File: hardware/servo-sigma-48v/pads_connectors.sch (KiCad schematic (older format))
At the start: 38 parts, among them J1 CONN_01X02, J3 CONN_01X03, J4 CONN_01X03_MALE, U1 ST1S14, U2 TPS70950, U3 ACS711, U8 TPS70933

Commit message: Updated the footprints
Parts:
- C1, C6, C9: footprint Capacitors_SMD:CP_Elec_10x10 -> Capacitor_SMD:CP_Elec_10x10; symbol device:CP -> servo-sigma-48v-rescue:CP-device
- C10, C12, C13, C37: footprint Capacitors_SMD:C_0603 -> Capacitor_SMD:C_0603_1608Metric; symbol device:C -> servo-sigma-48v-rescue:C-device
- C2, C7: footprint Capacitors_SMD:C_1206 -> Capacitor_SMD:C_1206_3216Metric; symbol device:C -> servo-sigma-48v-rescue:C-device
- C38: footprint Capacitors_SMD:CP_Elec_6.3x7.7 -> Capacitor_SMD:CP_Elec_6.3x7.7; symbol device:CP -> servo-sigma-48v-rescue:CP-device
- C39, C40, C41, C42, C5, C8: footprint Capacitors_SMD:C_0805 -> Capacitor_SMD:C_0805_2012Metric; symbol device:C -> servo-sigma-48v-rescue:C-device
- D2, D3, D5: symbol device:D_Schottky -> servo-sigma-48v-rescue:D_Schottky-device
- J1: symbol conn:CONN_01X02 -> servo-sigma-48v-rescue:CONN_01X02-conn
- J3: symbol conn:CONN_01X03 -> servo-sigma-48v-rescue:CONN_01X03-conn
- J4: footprint Pin_Headers:Pin_Header_Straight_1x03_Pitch2.54mm -> Connector_PinHeader_2.54mm:PinHeader_1x03_P2.54mm_Vertical; symbol conn:CONN_01X03_MALE -> servo-sigma-48v-rescue:CONN_01X03_MALE-conn
- L1: footprint Inductors_SMD:L_Wuerth_WE-TPC-3816 -> Inductor_SMD:L_Wuerth_WE-TPC-3816; symbol device:L -> servo-sigma-48v-rescue:L-device
- R11, R12, R13, R14, R15, R6, R7: footprint Resistors_SMD:R_0603 -> Resistor_SMD:R_0603_1608Metric; symbol device:R -> servo-sigma-48v-rescue:R-device
- U1: footprint Housings_SOIC:SOIC-8-1EP_3.9x4.9mm_Pitch1.27mm -> Package_SO:SOIC-8-1EP_3.9x4.9mm_P1.27mm_EP2.35x2.35mm
- U2, U8: footprint TO_SOT_Packages_SMD:SOT-23-5 -> Package_TO_SOT_SMD:SOT-23-5; symbol regul:TPS793333-EP -> servo-sigma-48v-rescue:TPS793333-EP-regul
- U3: footprint Housings_SOIC:SOIC-8_3.9x4.9mm_Pitch1.27mm -> Package_SO:SOIC-8_3.9x4.9mm_P1.27mm

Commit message: Work on sigmadrive 2.0
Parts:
- removed C10: 100nF 50V, Capacitor_SMD:C_0603_1608Metric, symbol servo-sigma-48v-rescue:C-device
- removed C5, C8: 1uF 100V, Capacitor_SMD:C_0805_2012Metric, symbol servo-sigma-48v-rescue:C-device
- removed R14: 10k, Resistor_SMD:R_0603_1608Metric, symbol servo-sigma-48v-rescue:R-device
- removed R15: 47k, Resistor_SMD:R_0603_1608Metric, symbol servo-sigma-48v-rescue:R-device
- removed U3: ACS711, Package_SO:SOIC-8_3.9x4.9mm_P1.27mm, symbol sigmadrone:ACS711
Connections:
- net labels removed: CURRENT_ADC_FILTERED, CURRENT_FAULT
- wire segments 151 -> 121
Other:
- note removed: "Low-pass filter, cutoff at 3.4 Hz"
- moved on the sheet: C1, C6, C9

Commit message: work on rs485
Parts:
- removed J4: CONN_01X03_MALE, Connector_PinHeader_2.54mm:PinHeader_1x03_P2.54mm_Vertical, symbol servo-sigma-48v-rescue:CONN_01X03_MALE-conn
- added J4: Conn_01x03, Connector_PinHeader_2.54mm:PinHeader_1x03_P2.54mm_Horizontal, symbol Connector_Generic:Conn_01x03
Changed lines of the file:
@@
 	-1   0    0    -1
-$EndComp
-$Comp
-L servo-sigma-48v-rescue:CONN_01X03_MALE-conn J4
-U 1 1 5BCC7E52
-P 1750 2100
-F 0 "J4" H 1856 2490 50  0000 C CNN
-F 1 "CONN_01X03_MALE" H 1856 2399 50  0000 C CNN
-F 2 "Connector_PinHeader_2.54mm:PinHeader_1x03_P2.54mm_Vertical" H 1750 2300 50  0001 C CNN
-F 3 "" H 1750 2300 50  0001 C CNN
-F 4 "732-5316-ND" H 1750 2100 50  0001 C CNN "Part"
-F 5 "DigiKey" H 1750 2100 50  0001 C CNN "Provider"
-	1    1750 2100
-	1    0    0    -1
 $EndComp
 Text Label 2900 1900 2    60   ~ 0
 PWM_IN
+Text Label 2900 2000 2    60   ~ 0
+PWM_5V
 Text Label 2900 2100 2    60   ~ 0
-PWM_5V
-Text Label 2900 2300 2    60   ~ 0
 PWM_GND
 Text HLabel 3000 1900 2    60   Output ~ 0
 PWM
-Wire Wire Line
-	2050 1900 3000 1900
 $Comp
 L power:GND #PWR045
 U 1 1 5BD194DC
-P 3000 2300
-F 0 "#PWR045" H 3000 2050 50  0001 C CNN
-F 1 "GND" H 3000 2150 50  0000 C CNN
-F 2 "" H 3000 2300 50  0001 C CNN
-F 3 "" H 3000 2300 50  0001 C CNN
-	1    3000 2300
-	0    -1   -1   0
-$EndComp
-Wire Wire Line
-	2050 2300 3000 2300
-$Comp
-L power:+5V #PWR043
-U 1 1 5BD23E44
 P 3000 2100
-F 0 "#PWR043" H 3000 1950 50  0001 C CNN
-F 1 "+5V" H 3015 2273 50  0000 C CNN
+F 0 "#PWR045" H 3000 1850 50  0001 C CNN
+F 1 "GND" V 3000 1900 50  0000 C CNN
 F 2 "" H 3000 2100 50  0001 C CNN
 F 3 "" H 3000 2100 50  0001 C CNN
 	1    3000 2100
+	0    -1   -1   0
+$EndComp
+$Comp
+L power:+5V #PWR043
+U 1 1 5BD23E44
+P 3000 2000
+F 0 "#PWR043" H 3000 1850 50  0001 C CNN
+F 1 "+5V" V 3000 2200 50  0000 C CNN
+F 2 "" H 3000 2000 50  0001 C CNN
+F 3 "" H 3000 2000 50  0001 C CNN
+	1    3000 2000
 	0    1    1    0
 $EndComp
-Wire Wire Line
-	2050 2100 3000 2100
 Wire Wire Line
 	3250 6950 3250 7650
@@
 	1    0    0    -1
 $EndComp
+$Comp
+L Connector_Generic:Conn_01x03 J?
+U 1 1 5CA52083
+P 1650 2000
+AR Path="/58BE2779/5CA52083" Ref="J?"  Part="1"
+AR Path="/58BE27E6/5CA52083" Ref="J4"  Part="1"
+F 0 "J4" H 1650 2200 50  0000 C CNN
+F 1 "Conn_01x03" H 1650 1800 50  0000 C CNN
+F 2 "Connector_PinHeader_2.54mm:PinHeader_1x03_P2.54mm_Horizontal" H 1650 2000 50  0001 C CNN
+F 3 "https://www.molex.com/pdm_docs/sd/705530002_sd.pdf" H 1650 2000 50  0001 C CNN
+F 4 "WM4901-ND" H 1650 2000 50  0001 C CNN "Part"
+F 5 "DigiKey" H 1650 2000 50  0001 C CNN "Provider"
+	1    1650 2000
+	-1   0    0    -1
+$EndComp
+Wire Wire Line
+	1850 1900 3000 1900
+Wire Wire Line
+	1850 2000 3000 2000
+Wire Wire Line
+	1850 2100 3000 2100
 $EndSCHEMATC

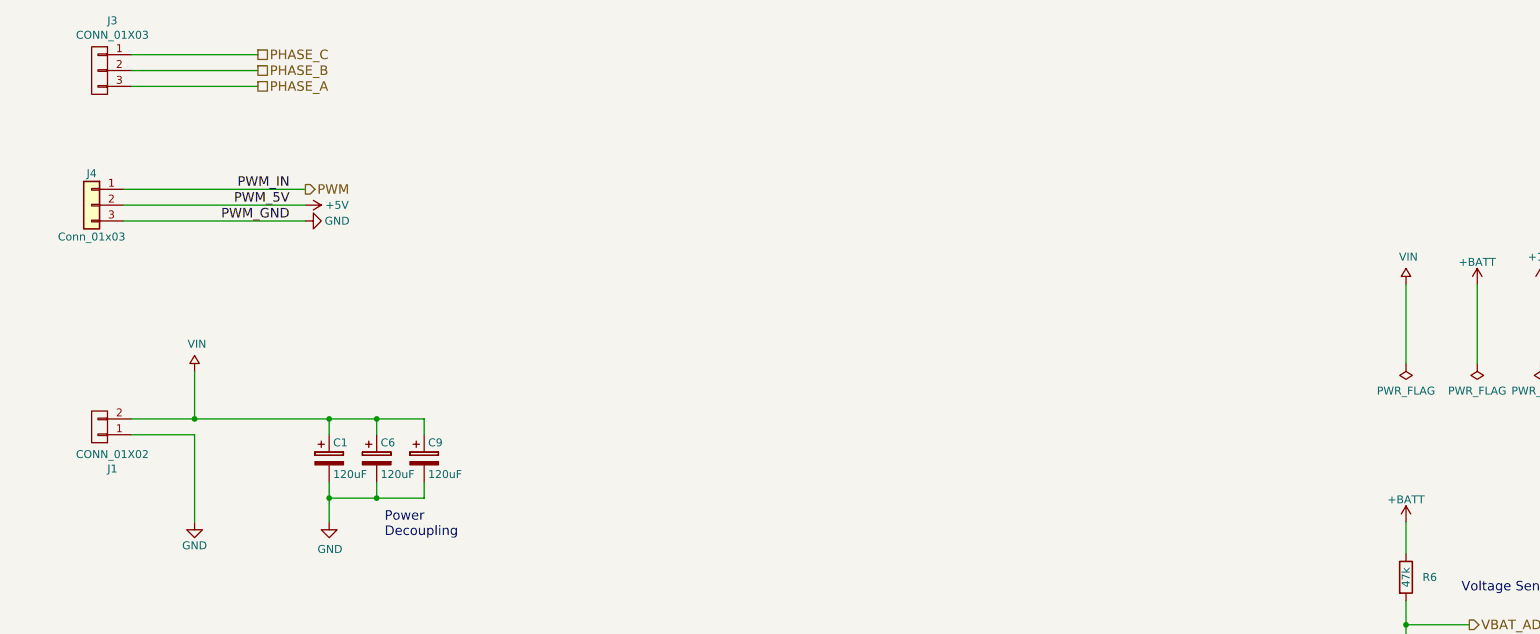
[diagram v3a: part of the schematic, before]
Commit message: Changed the MCU to use 100 pin
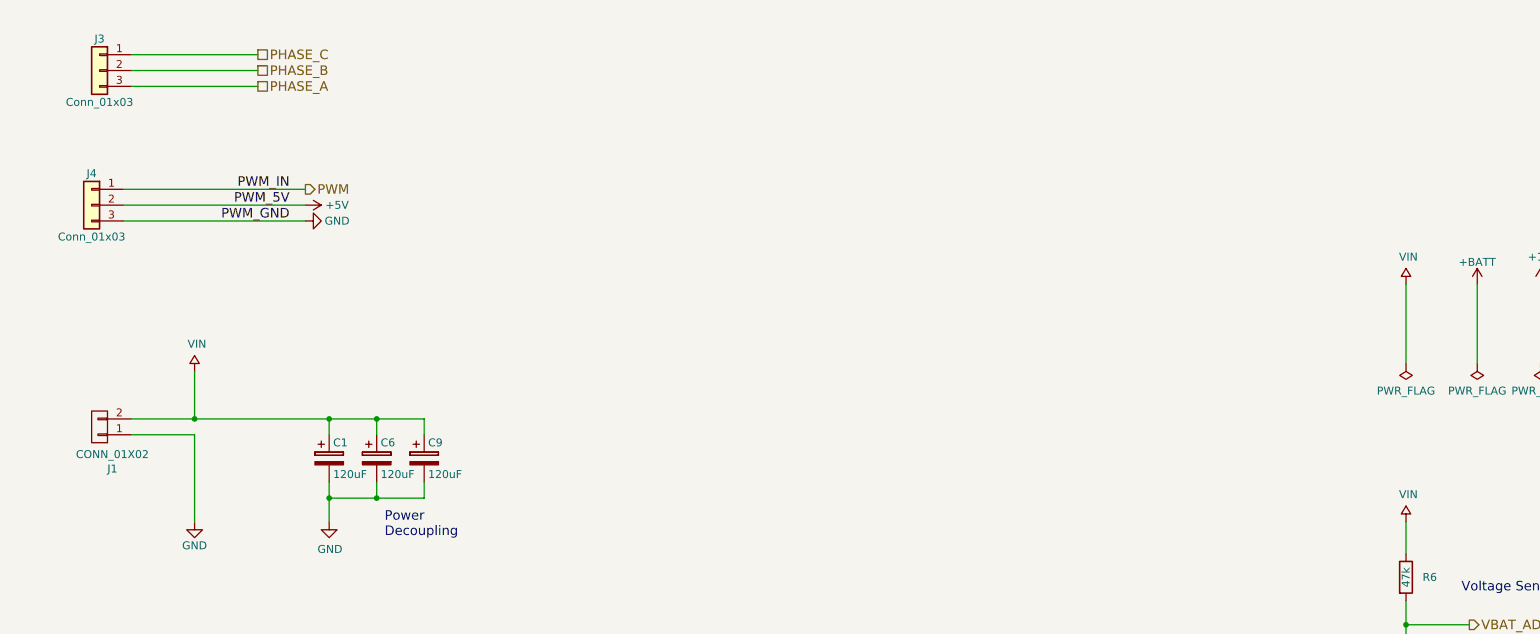
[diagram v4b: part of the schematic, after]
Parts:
- removed J3: CONN_01X03, Sigmadrone:PhoenixContact_MKDS_03x7.62mm_Vertical, symbol servo-sigma-48v-rescue:CONN_01X03-conn
- added J3: Conn_01x03, Connector_PinHeader_2.54mm:PinHeader_1x03_P2.54mm_Horizontal, symbol Connector_Generic:Conn_01x03
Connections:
- net +BATT: no longer R6.1
- net PHASE_A: now also J3.3 (Pin_3)
- net PHASE_B: now also J3.2 (Pin_2)
- net PHASE_C: now also J3.1 (Pin_1)
- net VIN: now also R6.1
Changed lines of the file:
@@
 	1    0    0    -1
-$EndComp
-$Comp
-L power:+BATT #PWR054
-U 1 1 58CF9E89
-P 9950 4000
-F 0 "#PWR054" H 9950 3850 50  0001 C CNN
-F 1 "+BATT" H 9950 4140 50  0000 C CNN
-F 2 "" H 9950 4000 50  0001 C CNN
-F 3 "" H 9950 4000 50  0001 C CNN
-	1    9950 4000
-	-1   0    0    -1
 $EndComp
 Text HLabel 10350 4650 2    60   Output ~ 0
@@
 Wire Wire Line
 	2700 1150 1900 1150
-$Comp
-L servo-sigma-48v-rescue:CONN_01X03-conn J3
-U 1 1 5BC83965
-P 1700 1150
-F 0 "J3" H 1619 1465 50  0000 C CNN
-F 1 "CONN_01X03" H 1619 1374 50  0000 C CNN
-F 2 "Sigmadrone:PhoenixContact_MKDS_03x7.62mm_Vertical" H 1700 1150 50  0001 C CNN
-F 3 "https://media.digikey.com/PDF/Data%20Sheets/Phoenix%20Contact%20PDFs/1704936.pdf" H 1700 1150 50  0001 C CNN
-F 4 "277-5954-ND" H 1700 1150 50  0001 C CNN "Part"
-F 5 "DigiKey" H 1700 1150 50  0001 C CNN "Provider"
-	1    1700 1150
-	-1   0    0    -1
-$EndComp
 Text Label 2900 1900 2    60   ~ 0
 PWM_IN
@@
 Wire Wire Line
 	1850 2100 3000 2100
+$Comp
+L sigmadrone:VIN #PWR0133
+U 1 1 5D195306
+P 9950 4000
+F 0 "#PWR0133" H 9950 3850 50  0001 C CNN
+F 1 "VIN" H 9965 4173 50  0000 C CNN
+F 2 "" H 9950 4000 50  0000 C CNN
+F 3 "" H 9950 4000 50  0000 C CNN
+	1    9950 4000
+	1    0    0    -1
+$EndComp
+$Comp
+L Connector_Generic:Conn_01x03 J?
+U 1 1 5DA2DCD3
+P 1700 1150
+AR Path="/58BE2779/5DA2DCD3" Ref="J?"  Part="1"
+AR Path="/58BE27E6/5DA2DCD3" Ref="J3"  Part="1"
+F 0 "J3" H 1700 1350 50  0000 C CNN
+F 1 "Conn_01x03" H 1700 950 50  0000 C CNN
+F 2 "Connector_PinHeader_2.54mm:PinHeader_1x03_P2.54mm_Horizontal" H 1700 1150 50  0001 C CNN
+F 3 "https://www.molex.com/pdm_docs/sd/705530002_sd.pdf" H 1700 1150 50  0001 C CNN
+F 4 "WM4901-ND" H 1700 1150 50  0001 C CNN "Part"
+F 5 "DigiKey" H 1700 1150 50  0001 C CNN "Provider"
+	1    1700 1150
+	-1   0    0    -1
+$EndComp
 $EndSCHEMATC

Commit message: Routed version 2.0
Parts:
- removed J3: Conn_01x03, Connector_PinHeader_2.54mm:PinHeader_1x03_P2.54mm_Horizontal, symbol Connector_Generic:Conn_01x03
- added J3: CONN_01X03, Sigmadrone:PhoenixContact_MKDS_03x7.62mm_Vertical, symbol servo-sigma-48v-rescue:CONN_01X03-conn
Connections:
- net PHASE_A: now also J3.3 (P3)
- net PHASE_B: now also J3.2 (P2)
- net PHASE_C: now also J3.1 (P1)
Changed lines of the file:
@@
 Wire Wire Line
 	2700 1150 1900 1150
+$Comp
+L servo-sigma-48v-rescue:CONN_01X03-conn J3
+U 1 1 5BC83965
+P 1700 1150
+F 0 "J3" H 1619 1465 50  0000 C CNN
+F 1 "CONN_01X03" H 1619 1374 50  0000 C CNN
+F 2 "Sigmadrone:PhoenixContact_MKDS_03x7.62mm_Vertical" H 1700 1150 50  0001 C CNN
+F 3 "https://media.digikey.com/PDF/Data%20Sheets/Phoenix%20Contact%20PDFs/1704936.pdf" H 1700 1150 50  0001 C CNN
+F 4 "277-5954-ND" H 1700 1150 50  0001 C CNN "Part"
+F 5 "DigiKey" H 1700 1150 50  0001 C CNN "Provider"
+	1    1700 1150
+	-1   0    0    -1
+$EndComp
 Text Label 2900 1900 2    60   ~ 0
 PWM_IN
@@
 Connection ~ 3250 7650
 $Comp
-L power:PWR_FLAG #FLG0101
-U 1 1 5BB0B70D
-P 10400 3000
-F 0 "#FLG0101" H 10400 3075 50  0001 C CNN
-F 1 "PWR_FLAG" H 10400 3173 50  0000 C CNN
-F 2 "" H 10400 3000 50  0001 C CNN
-F 3 "" H 10400 3000 50  0001 C CNN
-	1    10400 3000
-	-1   0    0    1
-$EndComp
-$Comp
-L power:+BATT #PWR0101
-U 1 1 5BB0B933
-P 10400 2500
-F 0 "#PWR0101" H 10400 2350 50  0001 C CNN
-F 1 "+BATT" H 10400 2640 50  0000 C CNN
-F 2 "" H 10400 2500 50  0001 C CNN
-F 3 "" H 10400 2500 50  0001 C CNN
-	1    10400 2500
-	-1   0    0    -1
-$EndComp
-$Comp
 L power:+15V #PWR0102
 U 1 1 5BB0BCCE
@@
 	-1   0    0    1
 $EndComp
-Wire Wire Line
-	10400 2500 10400 3000
 Wire Wire Line
 	10800 2500 10800 3000
@@
 $Comp
 L sigmadrone:VIN #PWR0133
-U 1 1 5D195306
+U 1 1 5CAF6219
 P 9950 4000
 F 0 "#PWR0133" H 9950 3850 50  0001 C CNN
@@
 	1    0    0    -1
 $EndComp
-$Comp
-L Connector_Generic:Conn_01x03 J?
-U 1 1 5DA2DCD3
-P 1700 1150
-AR Path="/58BE2779/5DA2DCD3" Ref="J?"  Part="1"
-AR Path="/58BE27E6/5DA2DCD3" Ref="J3"  Part="1"
-F 0 "J3" H 1700 1350 50  0000 C CNN
-F 1 "Conn_01x03" H 1700 950 50  0000 C CNN
-F 2 "Connector_PinHeader_2.54mm:PinHeader_1x03_P2.54mm_Horizontal" H 1700 1150 50  0001 C CNN
-F 3 "https://www.molex.com/pdm_docs/sd/705530002_sd.pdf" H 1700 1150 50  0001 C CNN
-F 4 "WM4901-ND" H 1700 1150 50  0001 C CNN "Part"
-F 5 "DigiKey" H 1700 1150 50  0001 C CNN "Provider"
-	1    1700 1150
-	-1   0    0    -1
-$EndComp
 $EndSCHEMATC

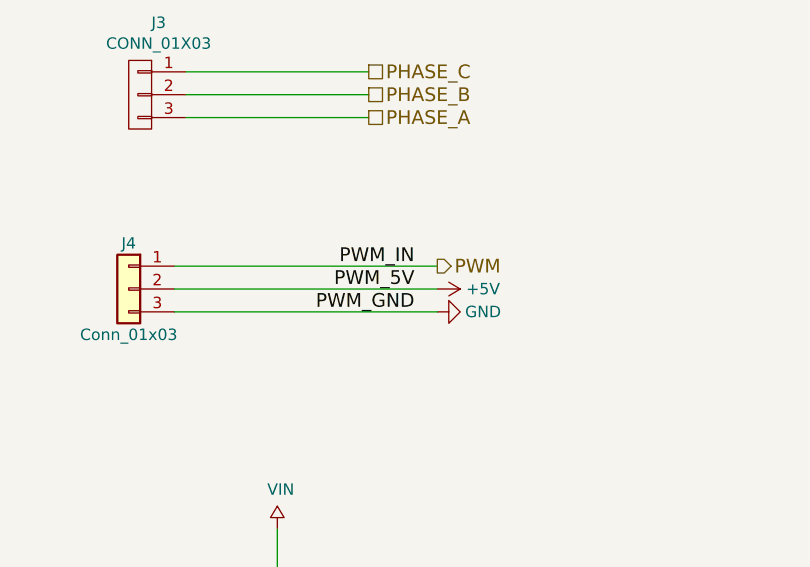
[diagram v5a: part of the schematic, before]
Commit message: Added NPTH for mounting heat sink.
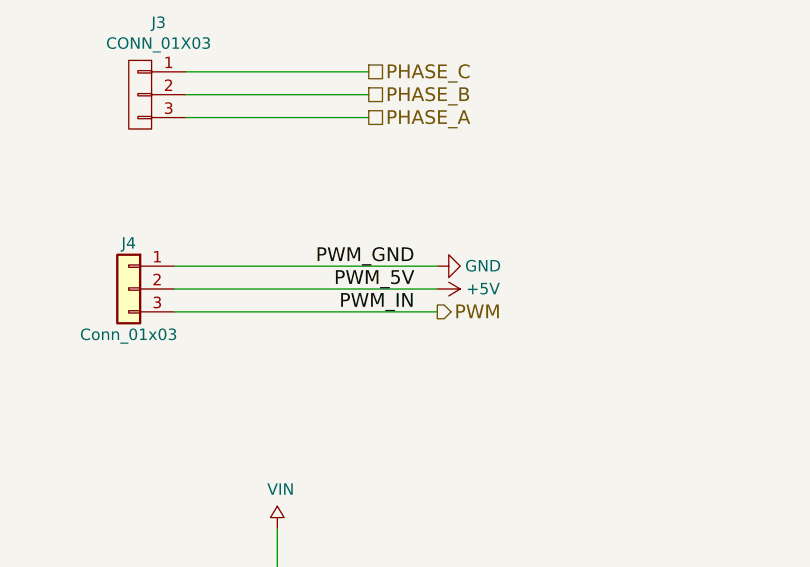
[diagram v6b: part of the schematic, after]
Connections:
- net GND: now also J4.1 (Pin_1); no longer J4.3 (Pin_3)
- net PWM: now also J4.3 (Pin_3); no longer J4.1 (Pin_1)
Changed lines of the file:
@@
 	-1   0    0    -1
 $EndComp
-Text Label 2900 1900 2    60   ~ 0
+Text Label 2900 2100 2    60   ~ 0
 PWM_IN
 Text Label 2900 2000 2    60   ~ 0
 PWM_5V
-Text Label 2900 2100 2    60   ~ 0
+Text Label 2900 1900 2    60   ~ 0
 PWM_GND
-Text HLabel 3000 1900 2    60   Output ~ 0
+Text HLabel 3000 2100 2    60   Output ~ 0
 PWM
 $Comp
 L power:GND #PWR045
 U 1 1 5BD194DC
-P 3000 2100
-F 0 "#PWR045" H 3000 1850 50  0001 C CNN
-F 1 "GND" V 3000 1900 50  0000 C CNN
-F 2 "" H 3000 2100 50  0001 C CNN
-F 3 "" H 3000 2100 50  0001 C CNN
-	1    3000 2100
+P 3000 1900
+F 0 "#PWR045" H 3000 1650 50  0001 C CNN
+F 1 "GND" V 3000 1700 50  0000 C CNN
+F 2 "" H 3000 1900 50  0001 C CNN
+F 3 "" H 3000 1900 50  0001 C CNN
+	1    3000 1900
 	0    -1   -1   0
 $EndComp
@@
 $EndComp
 Wire Wire Line
-	1850 1900 3000 1900
+	1850 2100 3000 2100
 Wire Wire Line
 	1850 2000 3000 2000
 Wire Wire Line
-	1850 2100 3000 2100
+	1850 1900 3000 1900
 $Comp
 L sigmadrone:VIN #PWR0133

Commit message: completed routing
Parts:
- removed J4: Conn_01x03, Connector_PinHeader_2.54mm:PinHeader_1x03_P2.54mm_Horizontal, symbol Connector_Generic:Conn_01x03
- renumbered C1 to C?, C13 to C?, C12 to C?, C2 to C?, C7 to C?, C38 to C?, C6 to C?, C9 to C?, C40 to C?, C39 to C?, C42 to C?, C41 to C?, D3 to D?, D2 to D?, F4 to F?, F3 to F?, F2 to F?, F1 to F?, J1 to J?, J3 to J?, L1 to L?, R6 to R?, R7 to R?, U1 to U?, U2 to U?, U8 to U?
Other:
- moved on the sheet: C?, F?, J?
